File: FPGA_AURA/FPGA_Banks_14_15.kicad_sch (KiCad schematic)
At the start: 1 part, among them U1 XC7A35T-2FTG256C

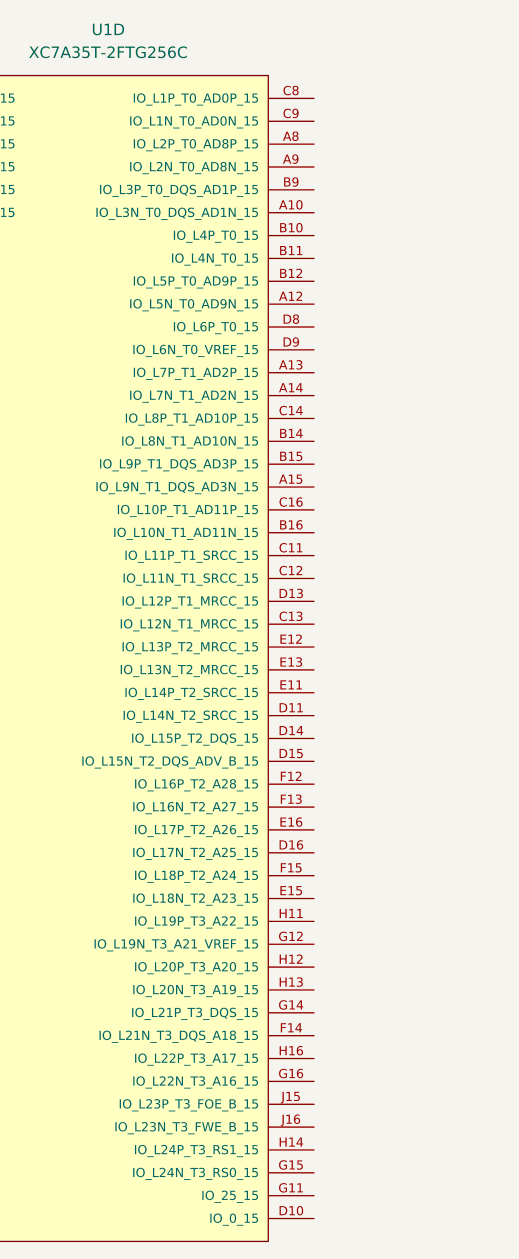
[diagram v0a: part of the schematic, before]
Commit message: Following new DDR3 reference
Using Scopefun v2 as a reference design for the XC7A35T-FTG256
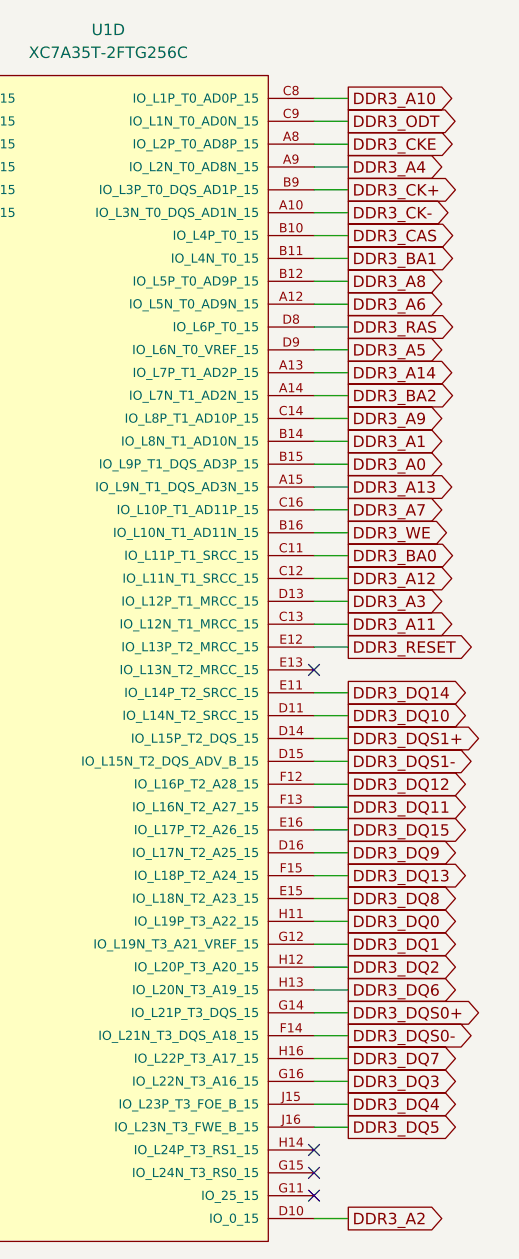
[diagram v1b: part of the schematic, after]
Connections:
- net DDR3_CK-: now reaches U1.A10 (IO_L3N_T0_DQS_AD1N_15)
- net DDR3_A6: now reaches U1.A12 (IO_L5N_T0_AD9N_15)
- net DDR3_A14: now reaches U1.A13 (IO_L7P_T1_AD2P_15)
- net DDR3_BA2: now reaches U1.A14 (IO_L7N_T1_AD2N_15)
- net DDR3_A13: now reaches U1.A15 (IO_L9N_T1_DQS_AD3N_15)
- net DDR3_CKE: now reaches U1.A8 (IO_L2P_T0_AD8P_15)
- net DDR3_A4: now reaches U1.A9 (IO_L2N_T0_AD8N_15)
- net DDR3_CAS: now reaches U1.B10 (IO_L4P_T0_15)
- net DDR3_BA1: now reaches U1.B11 (IO_L4N_T0_15)
- net DDR3_A8: now reaches U1.B12 (IO_L5P_T0_AD9P_15)
- net DDR3_A1: now reaches U1.B14 (IO_L8N_T1_AD10N_15)
- net DDR3_A0: now reaches U1.B15 (IO_L9P_T1_DQS_AD3P_15)
- net DDR3_WE: now reaches U1.B16 (IO_L10N_T1_AD11N_15)
- net DDR3_CK+: now reaches U1.B9 (IO_L3P_T0_DQS_AD1P_15)
- net DDR3_BA0: now reaches U1.C11 (IO_L11P_T1_SRCC_15)
- net DDR3_A12: now reaches U1.C12 (IO_L11N_T1_SRCC_15)
- net DDR3_A11: now reaches U1.C13 (IO_L12N_T1_MRCC_15)
- net DDR3_A9: now reaches U1.C14 (IO_L8P_T1_AD10P_15)
- net DDR3_A7: now reaches U1.C16 (IO_L10P_T1_AD11P_15)
- net DDR3_A10: now reaches U1.C8 (IO_L1P_T0_AD0P_15)
- net DDR3_ODT: now reaches U1.C9 (IO_L1N_T0_AD0N_15)
- net DDR3_A2: now reaches U1.D10 (IO_0_15)
- net DDR3_DQ10: now reaches U1.D11 (IO_L14N_T2_SRCC_15)
- net DDR3_A3: now reaches U1.D13 (IO_L12P_T1_MRCC_15)
- net DDR3_DQS1+: now reaches U1.D14 (IO_L15P_T2_DQS_15)
- net DDR3_DQS1-: now reaches U1.D15 (IO_L15N_T2_DQS_ADV_B_15)
- net DDR3_DQ9: now reaches U1.D16 (IO_L17N_T2_A25_15)
- net DDR3_RAS: now reaches U1.D8 (IO_L6P_T0_15)
- net DDR3_A5: now reaches U1.D9 (IO_L6N_T0_VREF_15)
- net DDR3_DQ14: now reaches U1.E11 (IO_L14P_T2_SRCC_15)
- net DDR3_RESET: now reaches U1.E12 (IO_L13P_T2_MRCC_15)
- net DDR3_DQ8: now reaches U1.E15 (IO_L18N_T2_A23_15)
- net DDR3_DQ15: now reaches U1.E16 (IO_L17P_T2_A26_15)
- net DDR3_DQ12: now reaches U1.F12 (IO_L16P_T2_A28_15)
- net DDR3_DQ11: now reaches U1.F13 (IO_L16N_T2_A27_15)
- net DDR3_DQS0-: now reaches U1.F14 (IO_L21N_T3_DQS_A18_15)
- net DDR3_DQ13: now reaches U1.F15 (IO_L18P_T2_A24_15)
- net DDR3_DQ1: now reaches U1.G12 (IO_L19N_T3_A21_VREF_15)
- net DDR3_DQS0+: now reaches U1.G14 (IO_L21P_T3_DQS_15)
- net DDR3_DQ3: now reaches U1.G16 (IO_L22N_T3_A16_15)
- net DDR3_DQ0: now reaches U1.H11 (IO_L19P_T3_A22_15)
- net DDR3_DQ2: now reaches U1.H12 (IO_L20P_T3_A20_15)
- net DDR3_DQ6: now reaches U1.H13 (IO_L20N_T3_A19_15)
- net DDR3_DQ7: now reaches U1.H16 (IO_L22P_T3_A17_15)
- net DDR3_DQ4: now reaches U1.J15 (IO_L23P_T3_FOE_B_15)
- net DDR3_DQ5: now reaches U1.J16 (IO_L23N_T3_FWE_B_15)
- no-connect marks 0 -> 4

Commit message: Moving to laptop
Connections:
- net DDR3_A14 is gone; now on net DDR3_A1: U1.A13 (IO_L7P_T1_AD2P_15)
- net DDR3_A0: now also U1.C8 (IO_L1P_T0_AD0P_15); no longer U1.B15 (IO_L9P_T1_DQS_AD3P_15)
- net DDR3_A1: no longer U1.B14 (IO_L8N_T1_AD10N_15)
- net DDR3_A10: now also U1.B10 (IO_L4P_T0_15); no longer U1.C8 (IO_L1P_T0_AD0P_15)
- net DDR3_A11: now also U1.A12 (IO_L5N_T0_AD9N_15); no longer U1.C13 (IO_L12N_T1_MRCC_15)
- net DDR3_A12: now also U1.B11 (IO_L4N_T0_15); no longer U1.C12 (IO_L11N_T1_SRCC_15)
- net DDR3_A13: now also U1.D8 (IO_L6P_T0_15); no longer U1.A15 (IO_L9N_T1_DQS_AD3N_15)
- net DDR3_A2: now also U1.C11 (IO_L11P_T1_SRCC_15); no longer U1.D10 (IO_0_15)
- net DDR3_A3: now also U1.C12 (IO_L11N_T1_SRCC_15); no longer U1.D13 (IO_L12P_T1_MRCC_15)
- net DDR3_A4: now also U1.B12 (IO_L5P_T0_AD9P_15); no longer U1.A9 (IO_L2N_T0_AD8N_15)
- net DDR3_A5: now also U1.D10 (IO_0_15); no longer U1.D9 (IO_L6N_T0_VREF_15)
- net DDR3_A6: now also U1.A15 (IO_L9N_T1_DQS_AD3N_15); no longer U1.A12 (IO_L5N_T0_AD9N_15)
- net DDR3_A7: now also U1.C9 (IO_L1N_T0_AD0N_15); no longer U1.C16 (IO_L10P_T1_AD11P_15)
- net DDR3_A8: now also U1.A14 (IO_L7N_T1_AD2N_15); no longer U1.B12 (IO_L5P_T0_AD9P_15)
- net DDR3_A9: now also U1.D9 (IO_L6N_T0_VREF_15); no longer U1.C14 (IO_L8P_T1_AD10P_15)
- net DDR3_BA0: now also U1.D13 (IO_L12P_T1_MRCC_15); no longer U1.C11 (IO_L11P_T1_SRCC_15)
- net DDR3_BA1: now also U1.B16 (IO_L10N_T1_AD11N_15); no longer U1.B11 (IO_L4N_T0_15)
- net DDR3_BA2: now also U1.A8 (IO_L2P_T0_AD8P_15); no longer U1.A14 (IO_L7N_T1_AD2N_15)
- net DDR3_CAS: now also U1.B15 (IO_L9P_T1_DQS_AD3P_15); no longer U1.B10 (IO_L4P_T0_15)
- net DDR3_CKE: now also U1.C16 (IO_L10P_T1_AD11P_15); no longer U1.A8 (IO_L2P_T0_AD8P_15)
- net DDR3_ODT: now also U1.C13 (IO_L12N_T1_MRCC_15); no longer U1.C9 (IO_L1N_T0_AD0N_15)
- net DDR3_RAS: now also U1.C14 (IO_L8P_T1_AD10P_15); no longer U1.D8 (IO_L6P_T0_15)
- net DDR3_WE: now also U1.A9 (IO_L2N_T0_AD8N_15); no longer U1.B16 (IO_L10N_T1_AD11N_15)
- no-connect marks 4 -> 6

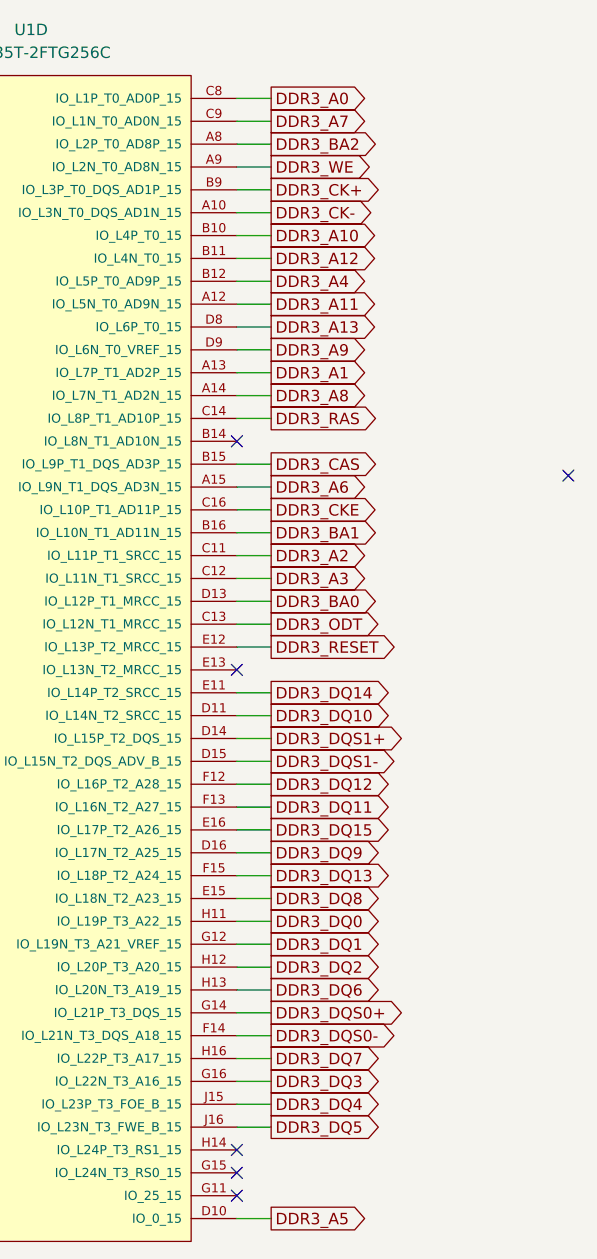
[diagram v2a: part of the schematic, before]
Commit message: Moved to KiCAD V10 for delay.
The FPGA PCB has now been moved to KiCAD V10 to make use of the new delay features and design rules are being setup.

PCB stack-up has now been decided.
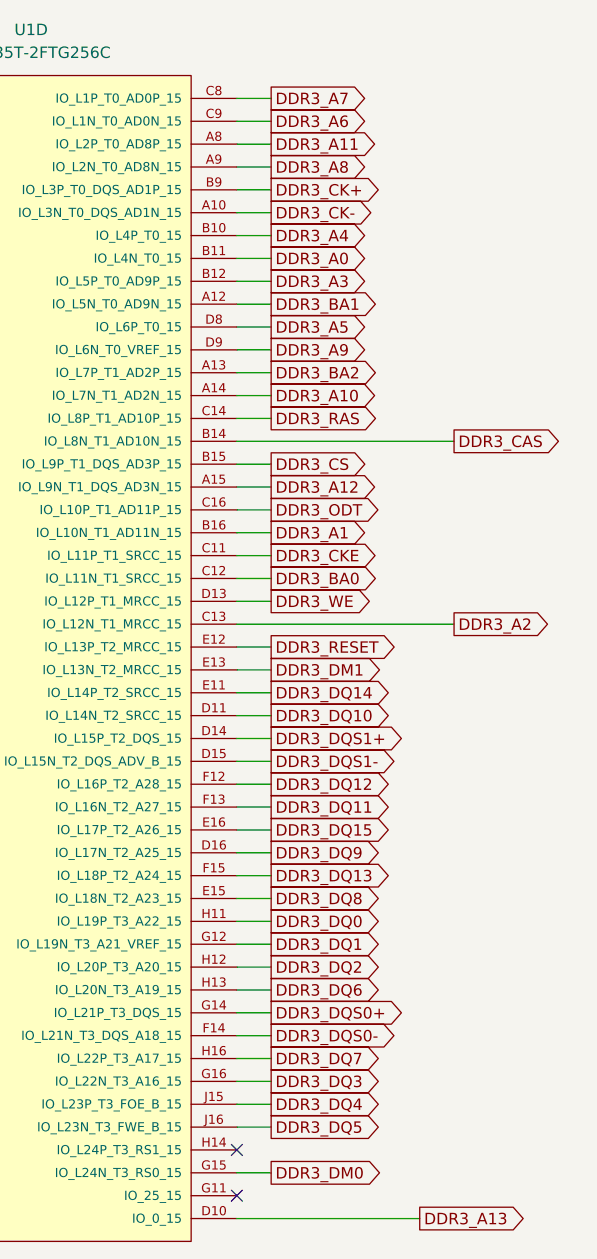
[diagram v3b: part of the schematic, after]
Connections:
- net DDR3_A0: now also U1.B11 (IO_L4N_T0_15); no longer U1.C8 (IO_L1P_T0_AD0P_15)
- net DDR3_A1: now also U1.B16 (IO_L10N_T1_AD11N_15); no longer U1.A13 (IO_L7P_T1_AD2P_15)
- net DDR3_A10: now also U1.A14 (IO_L7N_T1_AD2N_15); no longer U1.B10 (IO_L4P_T0_15)
- net DDR3_A11: now also U1.A8 (IO_L2P_T0_AD8P_15); no longer U1.A12 (IO_L5N_T0_AD9N_15)
- net DDR3_A12: now also U1.A15 (IO_L9N_T1_DQS_AD3N_15); no longer U1.B11 (IO_L4N_T0_15)
- net DDR3_A13: now also U1.D10 (IO_0_15); no longer U1.D8 (IO_L6P_T0_15)
- net DDR3_A2: now also U1.C13 (IO_L12N_T1_MRCC_15); no longer U1.C11 (IO_L11P_T1_SRCC_15)
- net DDR3_A3: now also U1.B12 (IO_L5P_T0_AD9P_15); no longer U1.C12 (IO_L11N_T1_SRCC_15)
- net DDR3_A4: now also U1.B10 (IO_L4P_T0_15); no longer U1.B12 (IO_L5P_T0_AD9P_15)
- net DDR3_A5: now also U1.D8 (IO_L6P_T0_15); no longer U1.D10 (IO_0_15)
- net DDR3_A6: now also U1.C9 (IO_L1N_T0_AD0N_15); no longer U1.A15 (IO_L9N_T1_DQS_AD3N_15)
- net DDR3_A7: now also U1.C8 (IO_L1P_T0_AD0P_15); no longer U1.C9 (IO_L1N_T0_AD0N_15)
- net DDR3_A8: now also U1.A9 (IO_L2N_T0_AD8N_15); no longer U1.A14 (IO_L7N_T1_AD2N_15)
- net DDR3_BA0: now also U1.C12 (IO_L11N_T1_SRCC_15); no longer U1.D13 (IO_L12P_T1_MRCC_15)
- net DDR3_BA1: now also U1.A12 (IO_L5N_T0_AD9N_15); no longer U1.B16 (IO_L10N_T1_AD11N_15)
- net DDR3_BA2: now also U1.A13 (IO_L7P_T1_AD2P_15); no longer U1.A8 (IO_L2P_T0_AD8P_15)
- net DDR3_CAS: now also U1.B14 (IO_L8N_T1_AD10N_15); no longer U1.B15 (IO_L9P_T1_DQS_AD3P_15)
- net DDR3_CKE: now also U1.C11 (IO_L11P_T1_SRCC_15); no longer U1.C16 (IO_L10P_T1_AD11P_15)
- net DDR3_ODT: now also U1.C16 (IO_L10P_T1_AD11P_15); no longer U1.C13 (IO_L12N_T1_MRCC_15)
- net DDR3_WE: now also U1.D13 (IO_L12P_T1_MRCC_15); no longer U1.A9 (IO_L2N_T0_AD8N_15)
- net DDR3_DM1: now reaches U1.E13 (IO_L13N_T2_MRCC_15)
- net DDR3_DM0: now reaches U1.G15 (IO_L24N_T3_RS0_15)
- new net DDR3_CS: U1.B15 (IO_L9P_T1_DQS_AD3P_15)
- no-connect marks 6 -> 2

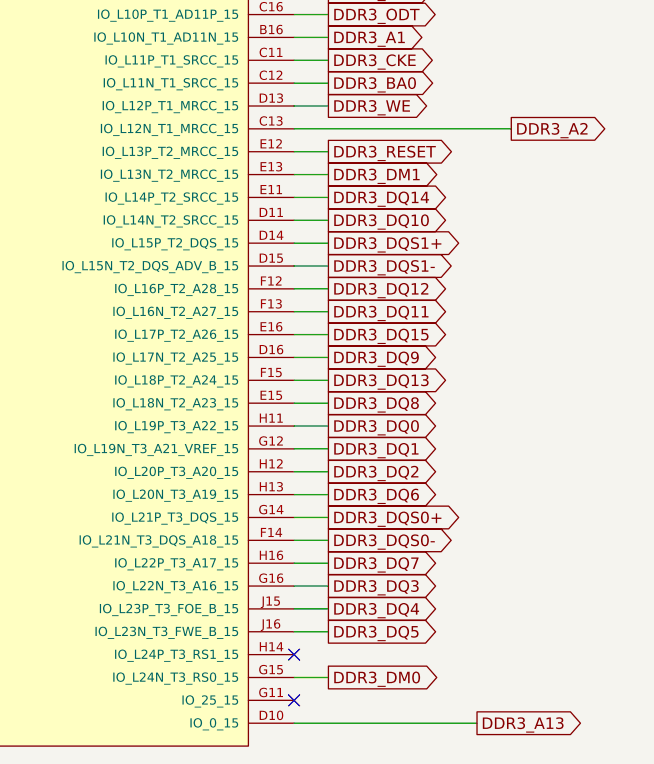
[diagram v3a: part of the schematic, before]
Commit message: Fixed delay matching issue and started data lines
The delay matching is now working again and the data byte lanes are in the process of being routed.
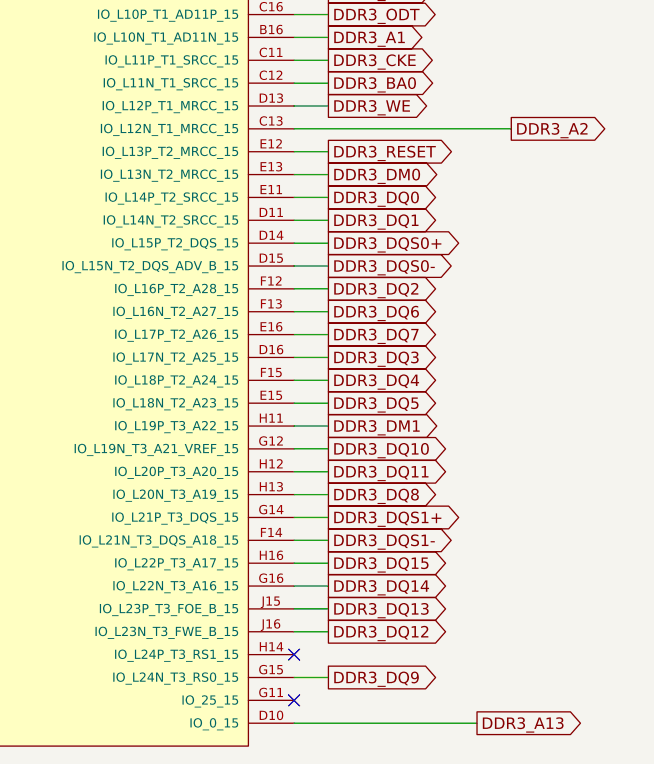
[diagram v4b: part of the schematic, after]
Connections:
- net DDR3_DM0: now also U1.E13 (IO_L13N_T2_MRCC_15); no longer U1.G15 (IO_L24N_T3_RS0_15)
- net DDR3_DM1: now also U1.H11 (IO_L19P_T3_A22_15); no longer U1.E13 (IO_L13N_T2_MRCC_15)
- net DDR3_DQ0: now also U1.E11 (IO_L14P_T2_SRCC_15); no longer U1.H11 (IO_L19P_T3_A22_15)
- net DDR3_DQ1: now also U1.D11 (IO_L14N_T2_SRCC_15); no longer U1.G12 (IO_L19N_T3_A21_VREF_15)
- net DDR3_DQ10: now also U1.G12 (IO_L19N_T3_A21_VREF_15); no longer U1.D11 (IO_L14N_T2_SRCC_15)
- net DDR3_DQ11: now also U1.H12 (IO_L20P_T3_A20_15); no longer U1.F13 (IO_L16N_T2_A27_15)
- net DDR3_DQ12: now also U1.J16 (IO_L23N_T3_FWE_B_15); no longer U1.F12 (IO_L16P_T2_A28_15)
- net DDR3_DQ13: now also U1.J15 (IO_L23P_T3_FOE_B_15); no longer U1.F15 (IO_L18P_T2_A24_15)
- net DDR3_DQ14: now also U1.G16 (IO_L22N_T3_A16_15); no longer U1.E11 (IO_L14P_T2_SRCC_15)
- net DDR3_DQ15: now also U1.H16 (IO_L22P_T3_A17_15); no longer U1.E16 (IO_L17P_T2_A26_15)
- net DDR3_DQ2: now also U1.F12 (IO_L16P_T2_A28_15); no longer U1.H12 (IO_L20P_T3_A20_15)
- net DDR3_DQ3: now also U1.D16 (IO_L17N_T2_A25_15); no longer U1.G16 (IO_L22N_T3_A16_15)
- net DDR3_DQ4: now also U1.F15 (IO_L18P_T2_A24_15); no longer U1.J15 (IO_L23P_T3_FOE_B_15)
- net DDR3_DQ5: now also U1.E15 (IO_L18N_T2_A23_15); no longer U1.J16 (IO_L23N_T3_FWE_B_15)
- net DDR3_DQ6: now also U1.F13 (IO_L16N_T2_A27_15); no longer U1.H13 (IO_L20N_T3_A19_15)
- net DDR3_DQ7: now also U1.E16 (IO_L17P_T2_A26_15); no longer U1.H16 (IO_L22P_T3_A17_15)
- net DDR3_DQ8: now also U1.H13 (IO_L20N_T3_A19_15); no longer U1.E15 (IO_L18N_T2_A23_15)
- net DDR3_DQ9: now also U1.G15 (IO_L24N_T3_RS0_15); no longer U1.D16 (IO_L17N_T2_A25_15)
- net DDR3_DQS0+: now also U1.D14 (IO_L15P_T2_DQS_15); no longer U1.G14 (IO_L21P_T3_DQS_15)
- net DDR3_DQS0-: now also U1.D15 (IO_L15N_T2_DQS_ADV_B_15); no longer U1.F14 (IO_L21N_T3_DQS_A18_15)
- net DDR3_DQS1+: now also U1.G14 (IO_L21P_T3_DQS_15); no longer U1.D14 (IO_L15P_T2_DQS_15)
- net DDR3_DQS1-: now also U1.F14 (IO_L21N_T3_DQS_A18_15); no longer U1.D15 (IO_L15N_T2_DQS_ADV_B_15)
